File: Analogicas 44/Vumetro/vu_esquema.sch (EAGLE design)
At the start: 3 parts

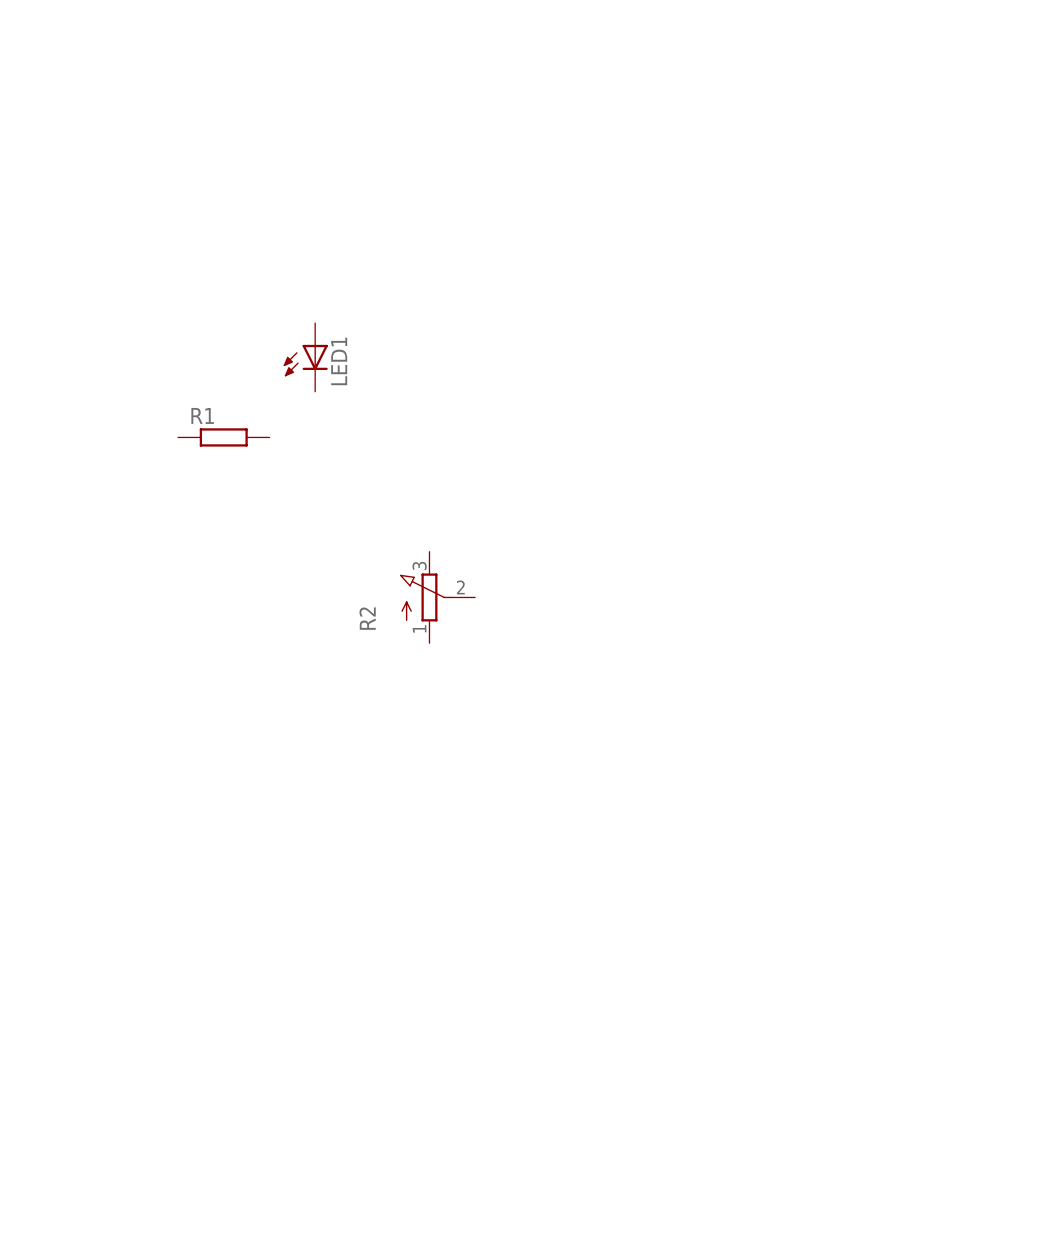
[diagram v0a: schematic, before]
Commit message: Vumetro con Arduino EEST N°2
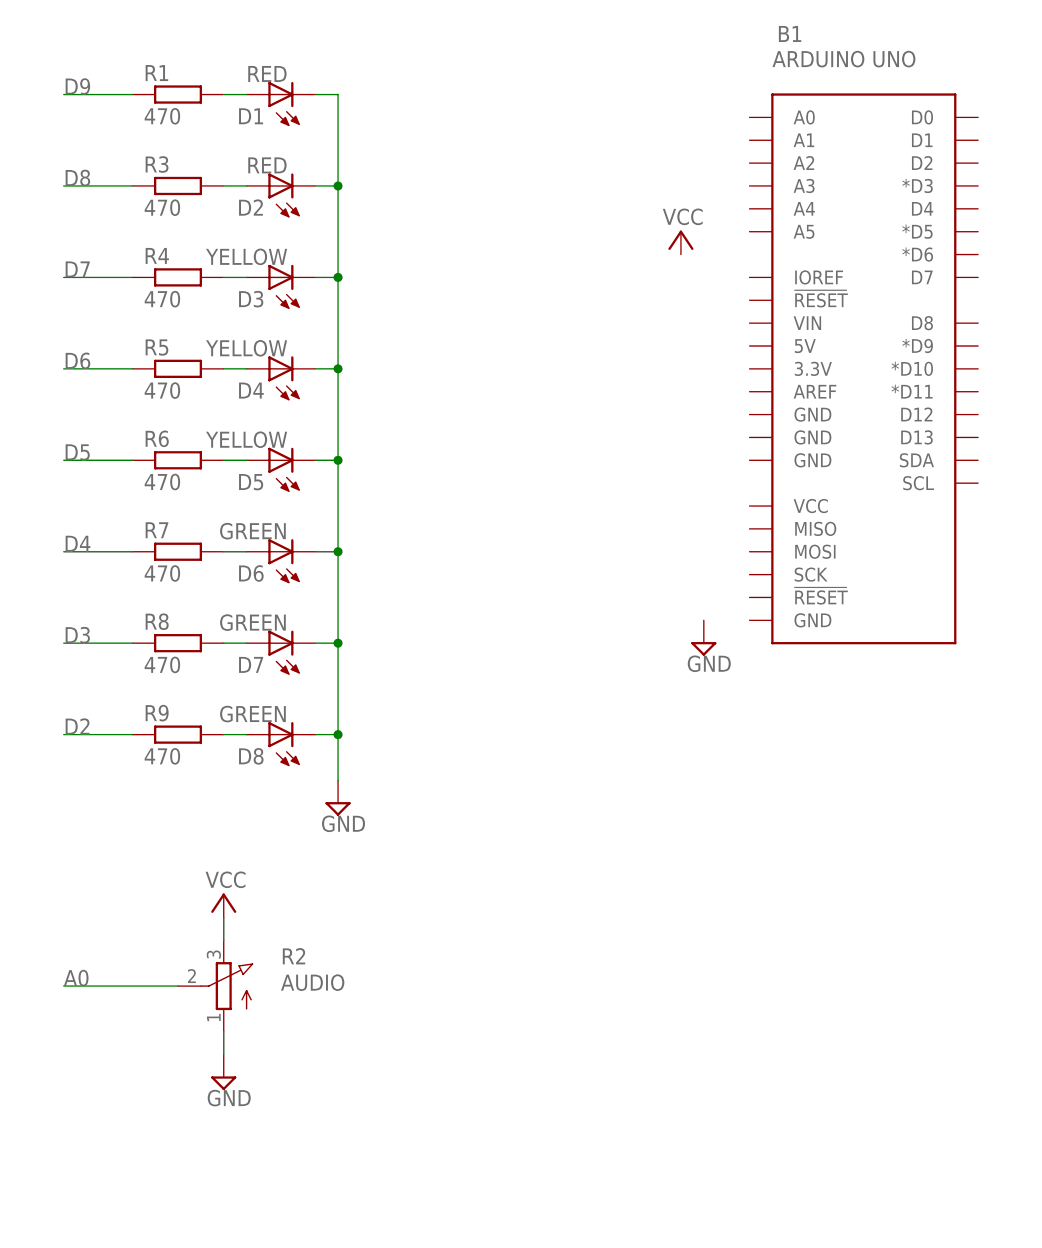
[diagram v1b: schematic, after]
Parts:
- removed LED1: (no value), treser_lib:LED5MM
- added B1: ARDUINO UNO, treser_lib:ARDUINO_UNO_R3
- added D1, D2: RED, treser_lib:LED5MM
- added D3, D4, D5: YELLOW, treser_lib:LED5MM
- added D6, D7, D8: GREEN, treser_lib:LED5MM
- added R3, R4, R5, R6, R7, R8, R9: 470, treser_lib:RESISTOR-EU0204/7
- R1: value (none) -> 470
- R2: value (none) -> AUDIO
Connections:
- new net A0: R2.S
- new net D2: R9.1
- new net D3: R8.1
- new net D4: R7.1
- new net D5: R6.1
- new net D6: R5.1
- new net D7: R4.1
- new net D8: R3.1
- new net D9: R1.1
- new net GND: D1.C, D2.C, D3.C, D4.C, D5.C, D6.C, D7.C, D8.C, R2.A
- new net N$2: D1.A, R1.2
- new net N$3: D2.A, R3.2
- new net N$4: D3.A, R4.2
- new net N$5: D4.A, R5.2
- new net N$6: D5.A, R6.2
- new net N$7: D6.A, R7.2
- new net N$8: D7.A, R8.2
- new net N$9: D8.A, R9.2
- new net VCC: R2.E
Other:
- moved on the sheet: R1, R2

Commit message: Vumetro con Arduino EEST N°2
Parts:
- added X1: POWER, treser_lib:BORNERA_AK500/2
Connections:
- net A0: now also B1.A0
- net D2: now also B1.D2
- net D3: now also B1.*D3
- net D4: now also B1.D4
- net D5: now also B1.*D5
- net D6: now also B1.*D6
- net D7: now also B1.D7
- net D8: now also B1.D8
- net D9: now also B1.*D9
- net GND: now also B1.GND, X1-1.KL
- net VCC: now also B1.5V, X1-2.KL
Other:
- moved on the sheet: B1, D1, D2, D3, D4, D5, D6, D7, D8, R1, R2, R3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
